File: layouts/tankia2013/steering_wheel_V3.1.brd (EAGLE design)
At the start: 100 x 70 mm, 92 parts, among them J1 1-292227-6, J2 1-292227-6, K1 USB-MICROZX62R-B, Q1 25 MHz, T1 FDC5614P, U1 STM32F415RG, U2 LMZ21701, U3 LMZ21701, U4 MAX6818, U5 NUF2221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

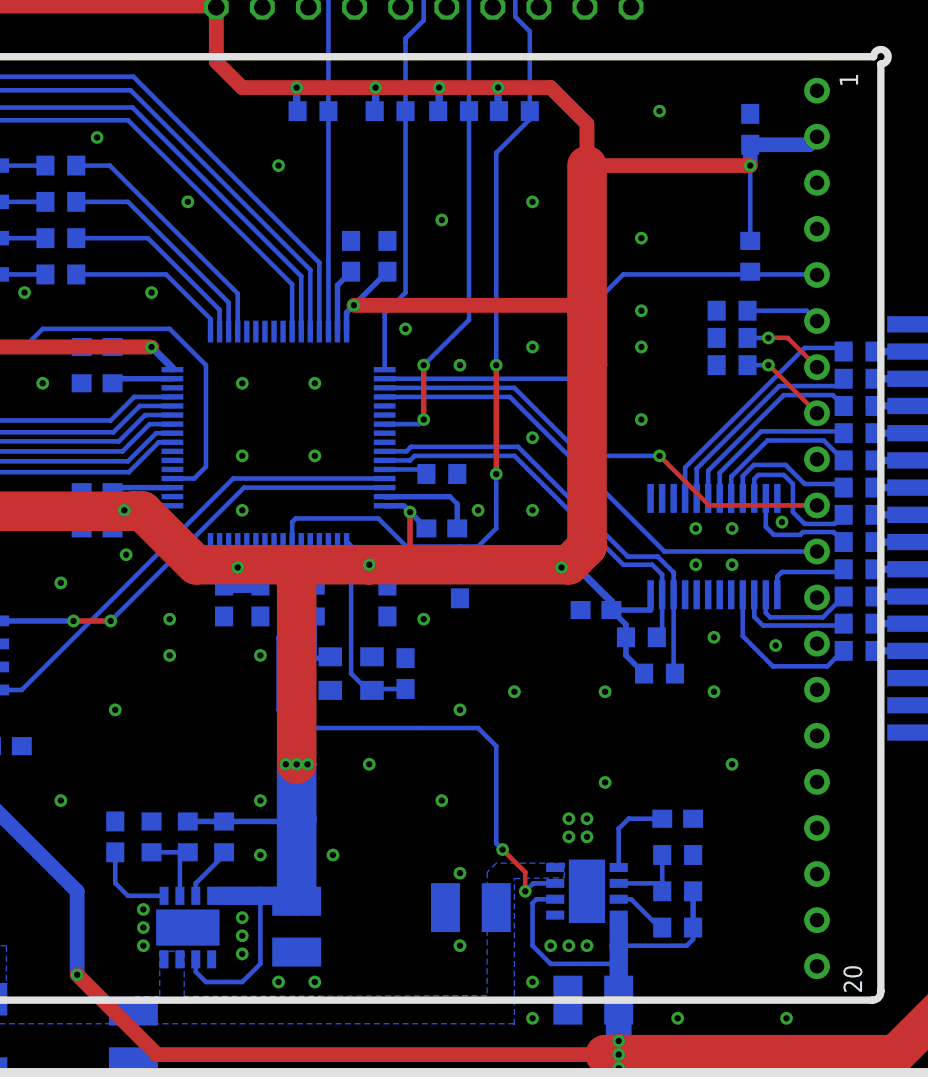
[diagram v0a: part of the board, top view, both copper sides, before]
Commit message: added stm32f7 breakout board
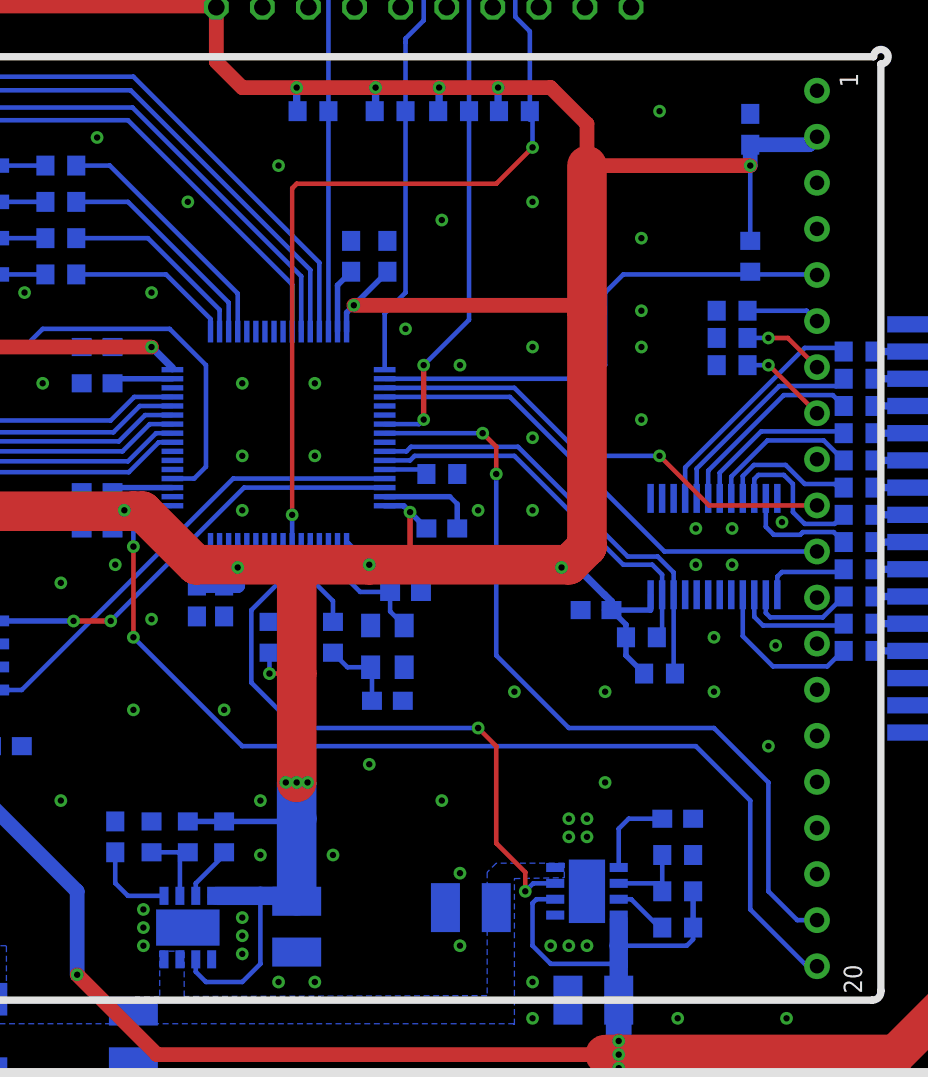
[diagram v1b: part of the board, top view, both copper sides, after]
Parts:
- moved R1 13.8 mm to (46.5, 29.0), turned to 90 degrees
- moved C13 9.49 mm to (48.0, 29.0)
- moved C6 5.22 mm to (53.0, 25.5), turned to 180 degrees
- moved C10 4.50 mm to (54.0, 31.5), turned to 180 degrees
- moved C8 3.50 mm to (42.5, 31.0)
- moved Q1 2.50 mm to (53.0, 28.5), turned to 270 degrees
- moved C5 2.24 mm to (54.0, 33.0), turned to 180 degrees
- moved R2 2.24 mm to (50.0, 29.0)
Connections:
- new net EDIP_DATA_READY: DISPLAY.P$20, U1.17
- new net EDIP_WRITE_PROTECTION: DISPLAY.P$19, U1.56
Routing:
- net EDIP_DATA_READY: track 0.00 -> 57.4 mm, vias 0 -> 2
- net EDIP_WRITE_PROTECTION: track 0.00 -> 45.2 mm, vias 0 -> 2
- net N$4: track 12.1 -> 9.41 mm
- net N$3: track 2.61 -> 5.02 mm
- net !RESET: track 49.5 -> 51.3 mm
- net EN_+5V: track 32.6 -> 33.8 mm
- net +3V3: track 322.0 -> 321.7 mm, vias 20 -> 21
- net GND: vias 137 -> 134

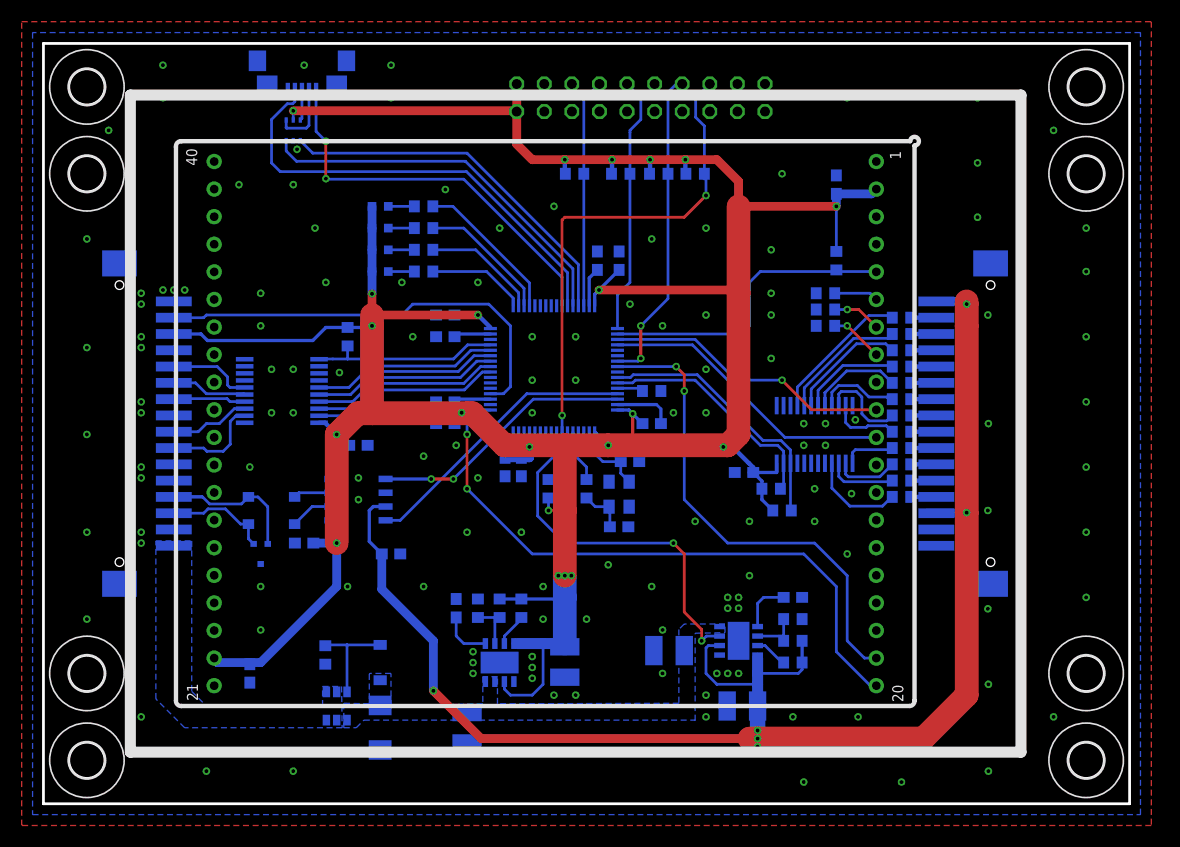
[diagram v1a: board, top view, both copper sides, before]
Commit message: updated layout, changed old 20 pin IDC to new 10 pin debug
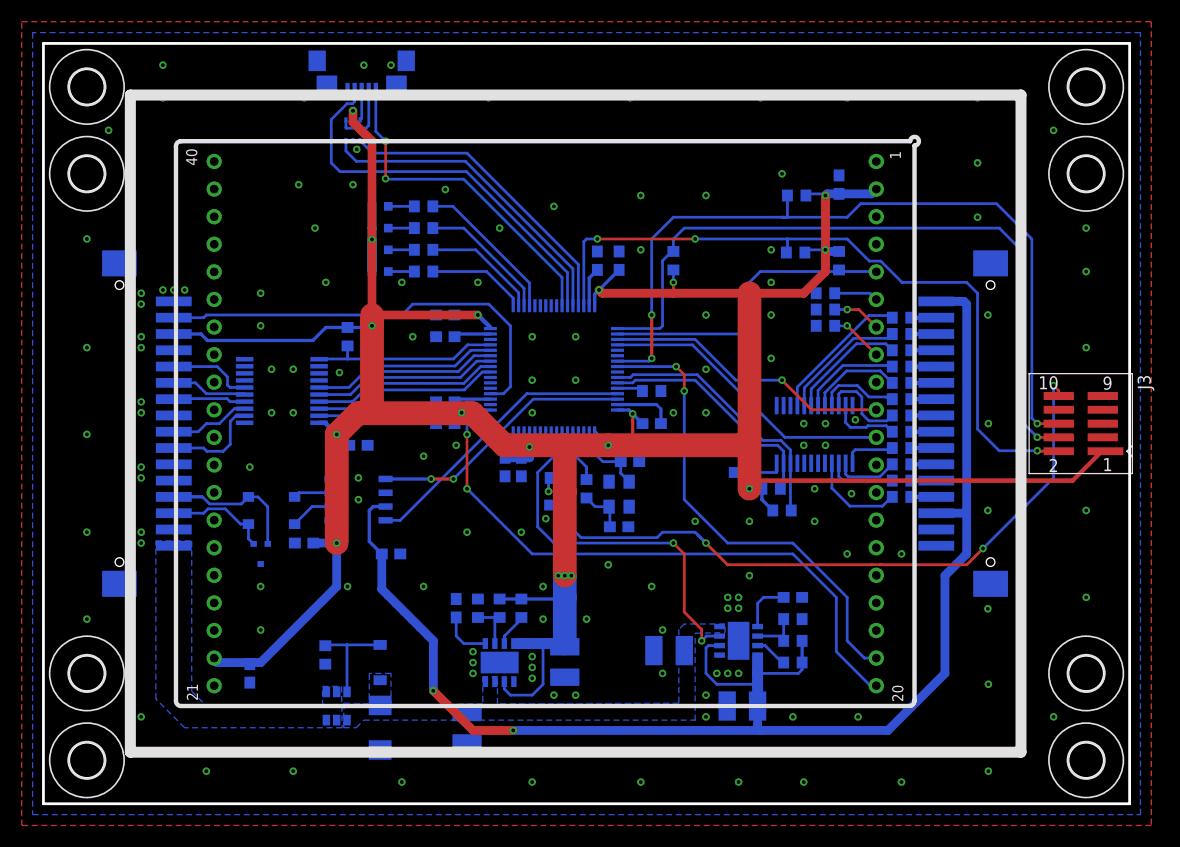
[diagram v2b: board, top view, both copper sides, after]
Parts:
- removed R19: x(10K), rcl:R0603
- removed SV1: (no value), con-ml:ML20
- added J3: FTSH-105-01-F-DV-K, samtec:FTSH-105-01-XXX-DV-K
- moved R22 21.6 mm to (69.2, 50.8), turned to 0 degrees
- moved R20 12.9 mm to (69.3, 56.0), turned to 0 degrees
- moved R21 9.36 mm to (58.0, 50.0), turned to 90 degrees
- moved K1 5.50 mm to (29.3, 68.0)
- moved U5 5.50 mm to (28.5, 62.0)
- moved C13 1.58 mm to (47.5, 27.5), turned to 0 degrees
- moved R1 1.41 mm to (47.5, 30.0), turned to 180 degrees
- moved C21 0.25 mm to (73.2, 57.0)
- moved R15 0.25 mm to (73.2, 50.0)
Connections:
- net !RESET: now also J3.10; no longer R19.2, SV1.15
- net +3V3: now also J3.1; no longer R19.1, SV1.1, SV1.2
- net GND: now also J3.3, J3.5; no longer SV1.10, SV1.12, SV1.14, SV1.16, SV1.18, SV1.20, SV1.4, SV1.6, SV1.8
- net SWCLK: now also J3.4; no longer SV1.9
- net SWDIO: now also J3.2; no longer SV1.7
- net SWO: now also J3.6; no longer SV1.13
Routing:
- net SWDIO: track 21.0 -> 66.4 mm, vias 0 -> 3
- net SWO: track 29.4 -> 73.6 mm, vias 2 -> 3
- net SWCLK: track 23.9 -> 65.8 mm, vias 0 -> 1
- net !RESET: track 51.3 -> 74.4 mm, vias 2 -> 3
- net +5V: track 142.9 -> 135.9 mm, vias 6 -> 2
- net USB_OTG_FS_VBUS: track 36.6 -> 31.1 mm
- net USB_OTG_FS_DP: track 34.1 -> 28.6 mm
- net USB_OTG_FS_ID: track 42.4 -> 36.9 mm
- net USB_OTG_FS_DM: track 35.2 -> 29.7 mm
- net EDIP_WRITE_PROTECTION: track 45.2 -> 44.0 mm
- net EN_+5V: track 33.8 -> 34.4 mm
- net EDIP_DATA_READY: track 57.4 -> 56.8 mm
- net +3V3: track 321.7 -> 321.9 mm, vias 21 -> 19
- net GND: vias 134 -> 139
